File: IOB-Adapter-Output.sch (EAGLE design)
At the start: 13 parts, among them Q1 MOSFET-N, Q2 MOSFET-N, Q3 MOSFET-N, Q4 MOSFET-N, Q5 MOSFET-N, Q6 MOSFET-N, Q7 MOSFET-N, Q8 MOSFET-N

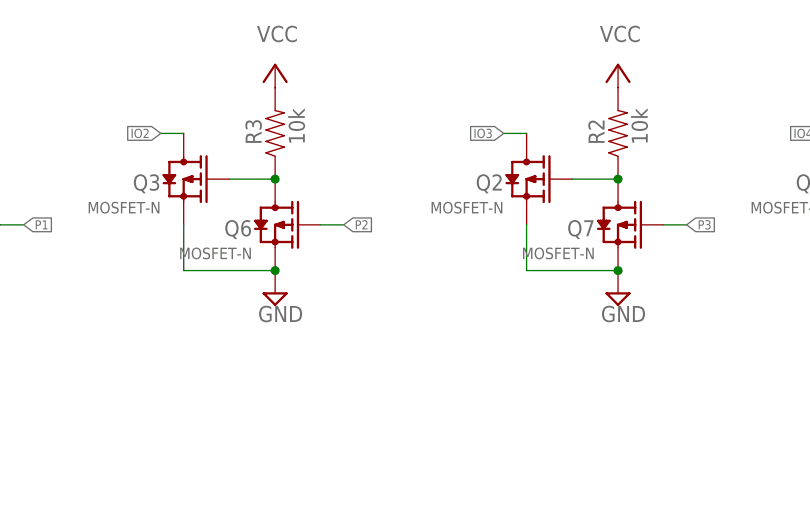
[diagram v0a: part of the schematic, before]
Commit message: typo in silkscreen
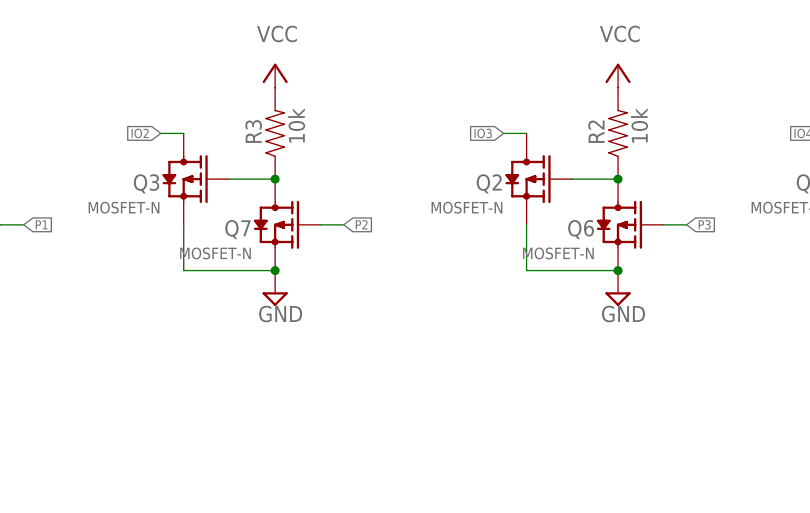
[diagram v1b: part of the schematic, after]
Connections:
- net N$6: now also Q7.D; no longer Q6.D
- net N$7: now also Q6.D; no longer Q7.D
- net P2: now also Q7.G; no longer Q6.G
- net P3: now also Q6.G; no longer Q7.G
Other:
- moved on the sheet: Q6, Q7
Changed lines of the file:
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@@
 <part name="R4" library="SPCoast" deviceset="R*" device="0805-RES" value="10k"/>
 <part name="P+2" library="supply1" deviceset="VCC" device=""/>
-<part name="Q6" library="SPCoast" deviceset="MOSFET-P" device="" value="MOSFET-N"/>
+<part name="Q7" library="SPCoast" deviceset="MOSFET-P" device="" value="MOSFET-N"/>
 <part name="V7" library="supply2" deviceset="GND" device=""/>
 <part name="Q3" library="SPCoast" deviceset="MOSFET-P" device="" value="MOSFET-N"/>
 <part name="R3" library="SPCoast" deviceset="R*" device="0805-RES" value="10k"/>
 <part name="P+7" library="supply1" deviceset="VCC" device=""/>
-<part name="Q7" library="SPCoast" deviceset="MOSFET-P" device="" value="MOSFET-N"/>
+<part name="Q6" library="SPCoast" deviceset="MOSFET-P" device="" value="MOSFET-N"/>
 <part name="V8" library="supply2" deviceset="GND" device=""/>
 <part name="Q2" library="SPCoast" deviceset="MOSFET-P" device="" value="MOSFET-N"/>
@@
 <attribute name="VALUE" x="58.42" y="144.78" size="1.778" layer="96" rot="MR0"/>
 </instance>
-<instance part="Q6" gate="Q" x="91.44" y="124.46" smashed="yes" rot="MR0">
+<instance part="Q7" gate="Q" x="91.44" y="124.46" smashed="yes" rot="MR0">
 <attribute name="NAME" x="88.9" y="123.19" size="1.778" layer="95" ratio="10" rot="MR0"/>
 <attribute name="VALUE" x="88.9" y="120.65" size="1.27" layer="96" ratio="10" rot="MR0"/>
@@
 <attribute name="VALUE" x="93.98" y="144.78" size="1.778" layer="96" rot="MR0"/>
 </instance>
-<instance part="Q7" gate="Q" x="129.54" y="124.46" smashed="yes" rot="MR0">
+<instance part="Q6" gate="Q" x="129.54" y="124.46" smashed="yes" rot="MR0">
 <attribute name="NAME" x="127" y="123.19" size="1.778" layer="95" ratio="10" rot="MR0"/>
 <attribute name="VALUE" x="127" y="120.65" size="1.27" layer="96" ratio="10" rot="MR0"/>
@@
 </segment>
 <segment>
-<pinref part="Q6" gate="Q" pin="S"/>
+<pinref part="Q7" gate="Q" pin="S"/>
 <pinref part="V7" gate="GND" pin="GND"/>
 <pinref part="Q3" gate="Q" pin="S"/>
@@
 </segment>
 <segment>
-<pinref part="Q7" gate="Q" pin="S"/>
+<pinref part="Q6" gate="Q" pin="S"/>
 <pinref part="V8" gate="GND" pin="GND"/>
 <pinref part="Q2" gate="Q" pin="S"/>
@@
 <wire x1="99.06" y1="124.46" x2="96.52" y2="124.46" width="0.1524" layer="91"/>
 <label x="99.06" y="124.46" size="1.016" layer="95" xref="yes"/>
-<pinref part="Q6" gate="Q" pin="G"/>
+<pinref part="Q7" gate="Q" pin="G"/>
 </segment>
 </net>
@@
 <wire x1="137.16" y1="124.46" x2="134.62" y2="124.46" width="0.1524" layer="91"/>
 <label x="137.16" y="124.46" size="1.016" layer="95" xref="yes"/>
-<pinref part="Q7" gate="Q" pin="G"/>
+<pinref part="Q6" gate="Q" pin="G"/>
 </segment>
 </net>
@@
 <net name="N$6" class="0">
 <segment>
-<pinref part="Q6" gate="Q" pin="D"/>
+<pinref part="Q7" gate="Q" pin="D"/>
 <pinref part="R3" gate="R" pin="1"/>
 <wire x1="91.44" y1="129.54" x2="86.36" y2="129.54" width="0.1524" layer="91"/>
@@
 <net name="N$7" class="0">
 <segment>
-<pinref part="Q7" gate="Q" pin="D"/>
+<pinref part="Q6" gate="Q" pin="D"/>
 <pinref part="R2" gate="R" pin="1"/>
 <wire x1="129.54" y1="129.54" x2="124.46" y2="129.54" width="0.1524" layer="91"/>

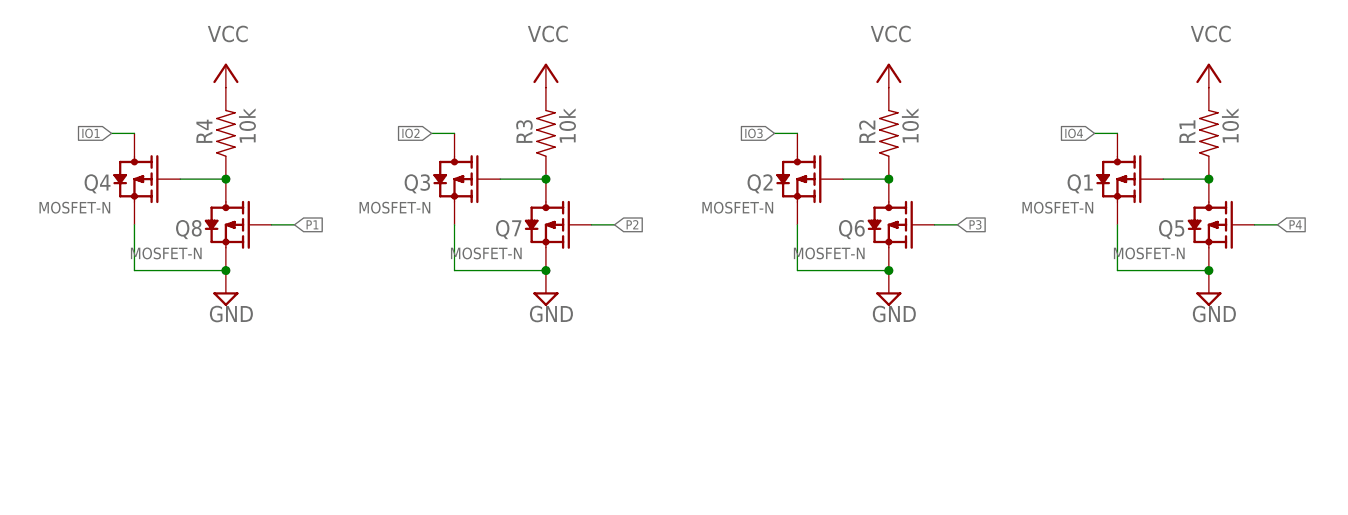
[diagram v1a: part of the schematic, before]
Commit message: normalized values
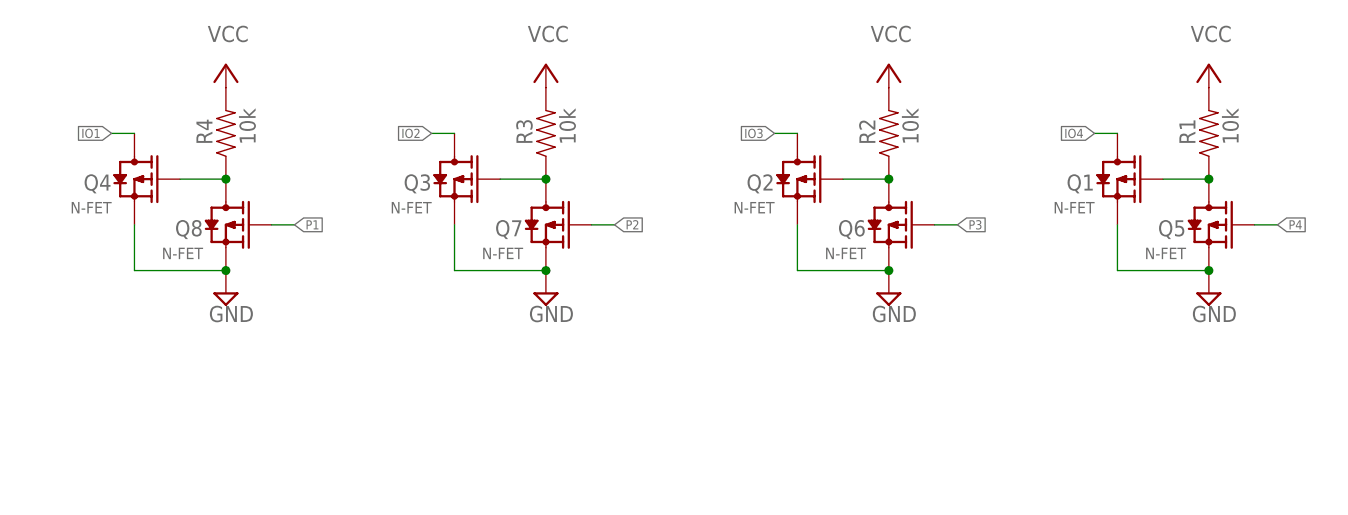
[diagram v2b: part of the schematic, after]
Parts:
- Q1, Q2, Q3, Q4, Q5, Q6, Q7, Q8: value MOSFET-N -> N-FET
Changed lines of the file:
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@@
 <part name="V1" library="supply2" deviceset="GND" device=""/>
 <part name="JP1" library="SPCoast" deviceset="CONNECTOR-M05X2" device="" value="CONNECTOR-M05X2"/>
-<part name="Q8" library="SPCoast" deviceset="MOSFET-P" device="" value="MOSFET-N"/>
+<part name="Q8" library="SPCoast" deviceset="MOSFET-P" device="" value="N-FET"/>
 <part name="V2" library="supply2" deviceset="GND" device=""/>
-<part name="Q4" library="SPCoast" deviceset="MOSFET-P" device="" value="MOSFET-N"/>
+<part name="Q4" library="SPCoast" deviceset="MOSFET-P" device="" value="N-FET"/>
 <part name="R4" library="SPCoast" deviceset="R*" device="0805-RES" value="10k"/>
 <part name="P+2" library="supply1" deviceset="VCC" device=""/>
-<part name="Q7" library="SPCoast" deviceset="MOSFET-P" device="" value="MOSFET-N"/>
+<part name="Q7" library="SPCoast" deviceset="MOSFET-P" device="" value="N-FET"/>
 <part name="V7" library="supply2" deviceset="GND" device=""/>
-<part name="Q3" library="SPCoast" deviceset="MOSFET-P" device="" value="MOSFET-N"/>
+<part name="Q3" library="SPCoast" deviceset="MOSFET-P" device="" value="N-FET"/>
 <part name="R3" library="SPCoast" deviceset="R*" device="0805-RES" value="10k"/>
 <part name="P+7" library="supply1" deviceset="VCC" device=""/>
-<part name="Q6" library="SPCoast" deviceset="MOSFET-P" device="" value="MOSFET-N"/>
+<part name="Q6" library="SPCoast" deviceset="MOSFET-P" device="" value="N-FET"/>
 <part name="V8" library="supply2" deviceset="GND" device=""/>
-<part name="Q2" library="SPCoast" deviceset="MOSFET-P" device="" value="MOSFET-N"/>
+<part name="Q2" library="SPCoast" deviceset="MOSFET-P" device="" value="N-FET"/>
 <part name="R2" library="SPCoast" deviceset="R*" device="0805-RES" value="10k"/>
 <part name="P+8" library="supply1" deviceset="VCC" device=""/>
-<part name="Q5" library="SPCoast" deviceset="MOSFET-P" device="" value="MOSFET-N"/>
+<part name="Q5" library="SPCoast" deviceset="MOSFET-P" device="" value="N-FET"/>
 <part name="V9" library="supply2" deviceset="GND" device=""/>
-<part name="Q1" library="SPCoast" deviceset="MOSFET-P" device="" value="MOSFET-N"/>
+<part name="Q1" library="SPCoast" deviceset="MOSFET-P" device="" value="N-FET"/>
 <part name="R1" library="SPCoast" deviceset="R*" device="0805-RES" value="10k"/>
 <part name="P+9" library="supply1" deviceset="VCC" device=""/>
